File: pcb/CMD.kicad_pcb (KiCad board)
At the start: 2 copper layers, 37.6 x 53.4 mm, 87 parts, among them J1 Conn_01x06_Pin, J2 Conn_01x06_Socket

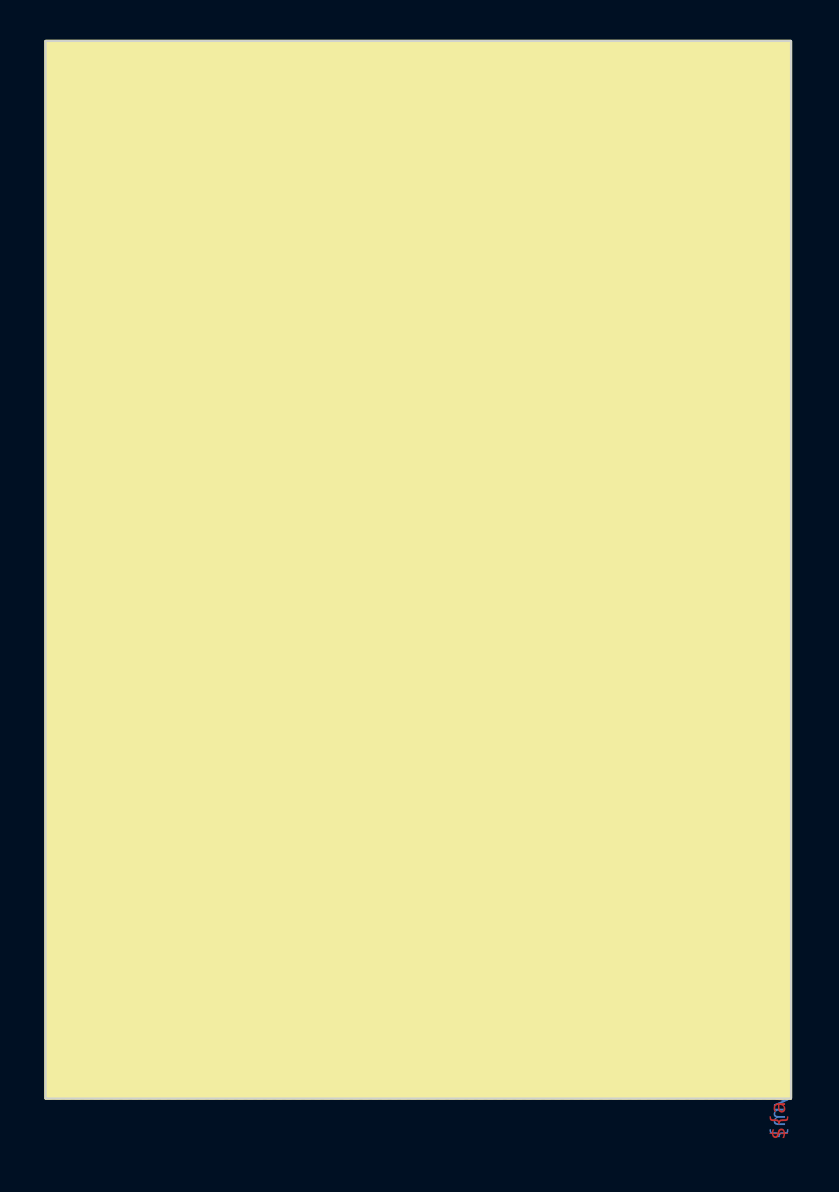
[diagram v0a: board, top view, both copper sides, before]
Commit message: Fix led position and add extended dimensioning
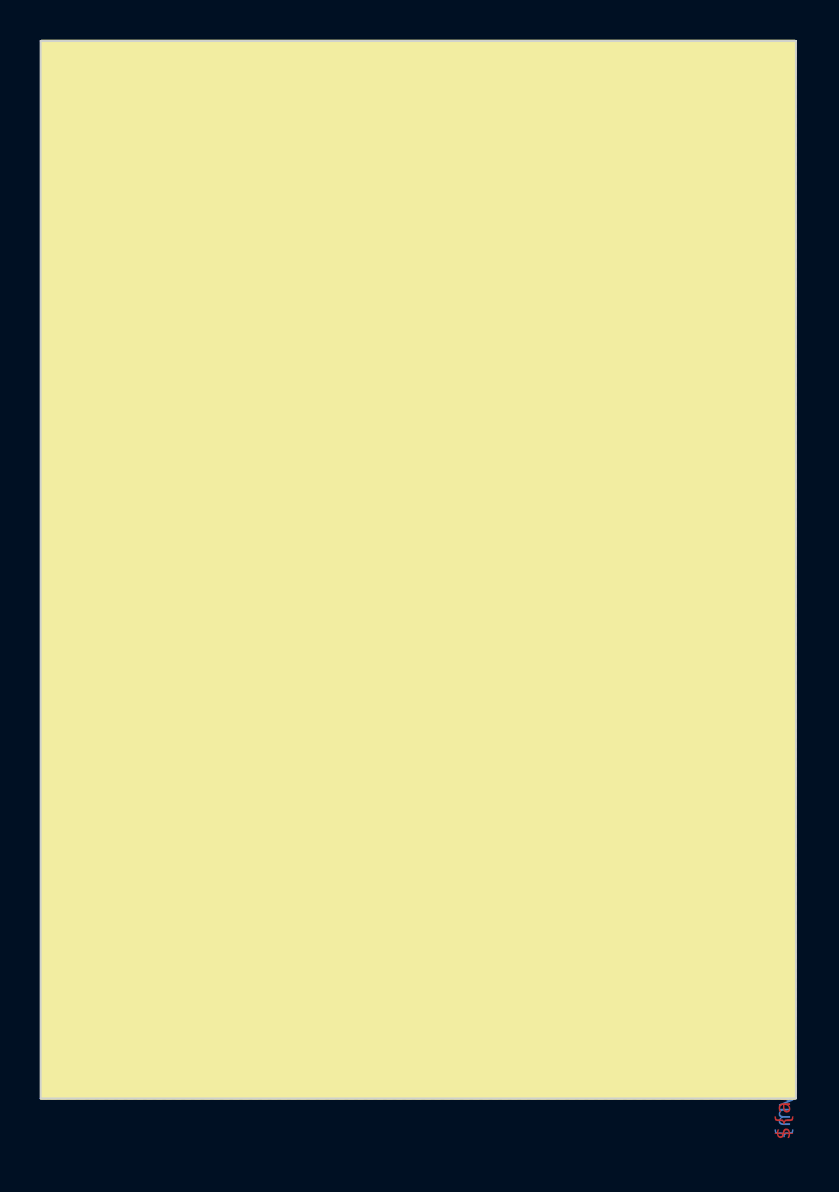
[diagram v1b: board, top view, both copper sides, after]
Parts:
- moved C29 0.25 mm to (159.6, 67.7)
- moved J2 0.25 mm to (160.8, 90.8)
- moved TP2 0.25 mm to (162.3, 113.0)
- moved C30 0.25 mm to (161.1, 77.5)
- moved C31 0.25 mm to (161.1, 80.6)
- moved C32 0.25 mm to (161.1, 100.3)
- moved C33 0.25 mm to (161.1, 102.9)
- moved C34 0.25 mm to (161.1, 107.4)
- moved D29 0.25 mm to (161.3, 67.3)
- moved D30 0.25 mm to (161.3, 74.9)
- moved D31 0.25 mm to (161.3, 82.5)
- moved D32 0.25 mm to (161.3, 90.2)
- moved D33 0.25 mm to (161.3, 97.8)
- moved D34 0.25 mm to (161.3, 105.4)
- moved D35 0.25 mm to (161.3, 113.0)
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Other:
- board size 37.6 x 53.4 mm -> 38.1 x 53.4 mm

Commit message: Lower pcb width
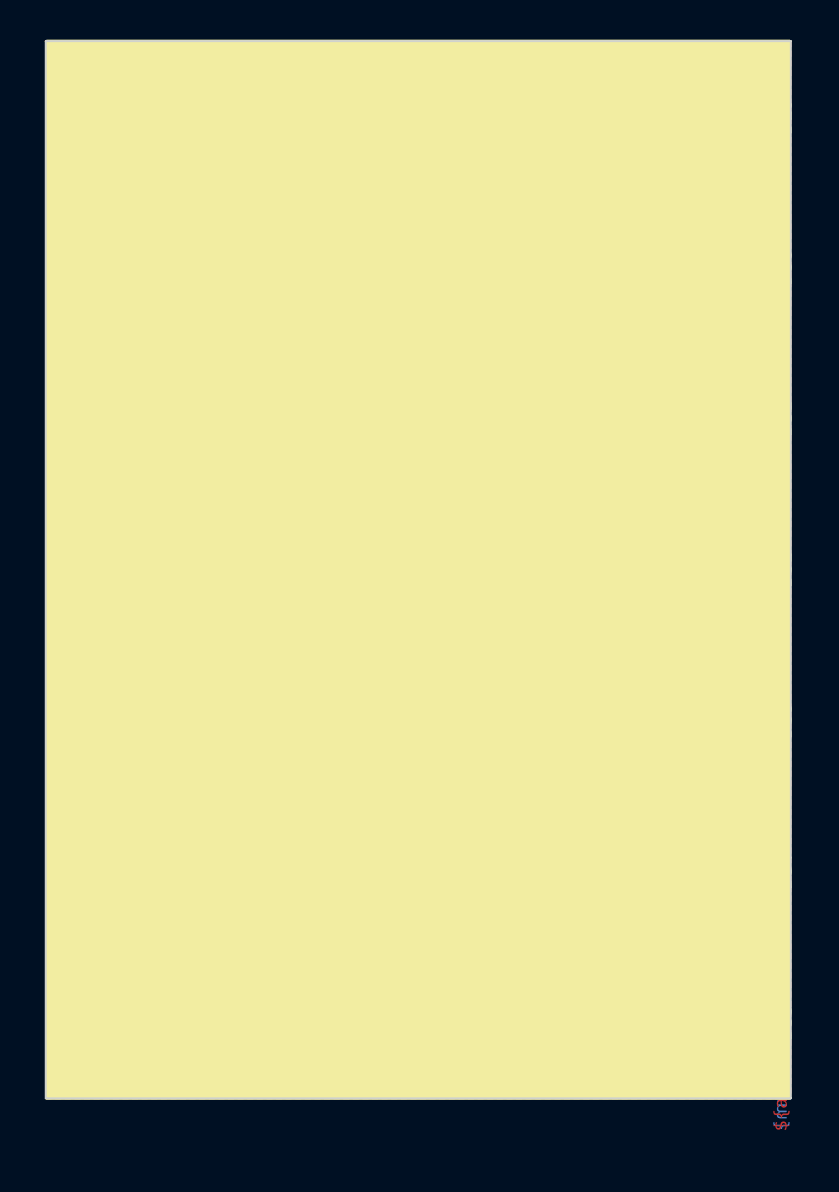
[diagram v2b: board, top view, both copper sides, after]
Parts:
- moved J1 0.26 mm to (128.3, 90.8)
- moved J2 0.25 mm to (160.5, 90.8)
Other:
- board size 38.1 x 53.4 mm -> 37.6 x 53.3 mm
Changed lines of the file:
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@@
     )
     (pad_to_mask_clearance 0)
-    (aux_axis_origin 127.004 63.495)
-    (grid_origin 127.004 63.495)
+    (aux_axis_origin 127.258 63.495)
+    (grid_origin 127.258 63.495)
     (pcbplotparams
       (layerselection 0x0010000_7ffffffe)
@@
   )
   (footprint "Connector_SMD:HARWIN_M20-8890645_Pin_Header" (layer "B.Cu")
-    (at 128.0415 90.796 90)
+    (at 128.2995 90.796 90)
     (property "Sheetfile" "CMD.kicad_sch")
     (property "Sheetname" "")
@@
   )
   (footprint "Connector_SMD:HARWIN_M20-7910642R_Pin_Socket" (layer "B.Cu")
-    (at 160.782 90.796 -90)
+    (at 160.532 90.796 -90)
     (property "Sheetfile" "CMD.kicad_sch")
     (property "Sheetname" "")
@@
   (gr_line (start 149.352 73.396) (end 145.542 73.396)
     (stroke (width 0.15) (type default)) (layer "B.SilkS"))
-  (gr_rect (start 127.054 63.495) (end 165.046 116.835)
+  (gr_rect (start 127.308 63.495) (end 164.792 116.835)
     (stroke (width 0.15) (type solid)) (fill solid) (layer "F.SilkS"))
-  (gr_rect (start 127 63.49) (end 165.1082 116.84)
+  (gr_rect (start 127.258 63.495) (end 164.85 116.835)
     (stroke (width 0.1) (type default)) (fill none) (layer "Edge.Cuts"))
   (gr_rect (start 120.904 83.053) (end 128.27 98.547)
     (stroke (width 0.15) (type default)) (fill none) (layer "User.1"))
-  (gr_text "${acronym}" (at 164.465 115.687 90) (layer "F.Cu")
-    (effects (font (size 0.75 0.75) (thickness 0.12)))
+  (gr_text "${acronym}" (at 164.342 115.687 90) (layer "F.Cu")
+    (effects (font (size 0.65 0.65) (thickness 0.12)))
   )
-  (gr_text "${acronym}" (at 164.465 115.687 90) (layer "B.Cu")
-    (effects (font (size 0.75 0.75) (thickness 0.12)) (justify mirror))
+  (gr_text "${acronym}" (at 164.342 115.687 90) (layer "B.Cu")
+    (effects (font (size 0.65 0.65) (thickness 0.12)) (justify mirror))
   )
   (gr_text "X" (at 141.478 87.112) (layer "B.SilkS")
@@
   )
   (dimension (type aligned) (layer "Dwgs.User")
-    (pts (xy 127.004 63.495) (xy 165.1042 63.495))
-    (height -3.81)
-    (gr_text "38.10" (at 146.0541 58.535) (layer "Dwgs.User")
+    (pts (xy 127.258 116.835) (xy 127.258 63.495))
+    (height -7.874)
+    (gr_text "53.34" (at 118.234 90.165 90) (layer "Dwgs.User")
       (effects (font (size 1 1) (thickness 0.15)))
     )
@@
   )
   (dimension (type aligned) (layer "Dwgs.User")
-    (pts (xy 127.254 63.495) (xy 127.254 116.84))
-    (height 11.43)
-    (gr_text "53.34" (at 114.674 90.1675 90) (layer "Dwgs.User")
-      (effects (font (size 1 1) (thickness 0.15)))
-    )
-    (format (prefix "") (suffix "") (units 3) (units_format 0) (precision 2))
-    (style (thickness 0.15) (arrow_length 1.27) (text_position_mode 0) (extension_height 0.58642) (extension_offset 0.5) keep_text_aligned)
-  )
-  (dimension (type aligned) (layer "User.1")
-    (pts (xy 130.81 113.025) (xy 127 113.025))
-    (height 50.8)
-    (gr_text "3.81" (at 128.905 61.075) (layer "User.1")
+    (pts (xy 127.258 63.495) (xy 164.8502 63.495))
+    (height -1.27)
+    (gr_text "37.59" (at 146.0541 61.075) (layer "Dwgs.User")
       (effects (font (size 1 1) (thickness 0.15)))
     )
@@
   )
   (dimension (type aligned) (layer "User.1")
-    (pts (xy 161.29 109.215) (xy 165.1 109.215))
-    (height -46.99)
-    (gr_text "3.81" (at 163.195 61.075) (layer "User.1")
+    (pts (xy 161.29 109.215) (xy 153.67 109.215))
+    (height 46.99)
+    (gr_text "7.62" (at 157.48 61.075) (layer "User.1")
       (effects (font (size 1 1) (thickness 0.15)))
     )
@@
   )
   (dimension (type aligned) (layer "User.1")
-    (pts (xy 161.29 109.215) (xy 153.67 109.215))
-    (height 46.99)
-    (gr_text "7.62" (at 157.48 61.075) (layer "User.1")
+    (pts (xy 161.29 113.025) (xy 164.85 113.025))
+    (height -50.8)
+    (gr_text "3.56" (at 163.07 61.075) (layer "User.1")
       (effects (font (size 1 1) (thickness 0.15)))
     )
@@
   )
   (dimension (type aligned) (layer "User.1")
+    (pts (xy 130.81 113.025) (xy 127.258 113.025))
+    (height 50.8)
+    (gr_text "3.56" (at 129.034 61.075) (layer "User.1")
+      (effects (font (size 1 1) (thickness 0.15)))
+    )
+    (format (prefix "") (suffix "") (units 3) (units_format 0) (precision 2) (override_value "3.56"))
+    (style (thickness 0.15) (arrow_length 1.27) (text_position_mode 0) (extension_height 0.58642) (extension_offset 0.5) keep_text_aligned)
+  )
+  (dimension (type aligned) (layer "User.1")
     (pts (xy 130.81 82.545) (xy 130.81 90.165))
     (height -37.084)
@@
   (segment (start 130.81 65.776) (end 130.81 64.905) (width 0.4) (layer "F.Cu") (net 5))
   (via (at 131.826 66.792) (size 0.4) (drill 0.3) (layers "F.Cu" "B.Cu") (net 5))
+  (segment (start 133.984 92.066) (end 131.9145 92.066) (width 0.4) (layer "B.Cu") (net 5))
   (segment (start 131.826 66.792) (end 133.35 66.792) (width 0.4) (layer "B.Cu") (net 5))
   (segment (start 135.128 68.57) (end 135.128 90.922) (width 0.4) (layer "B.Cu") (net 5))
-  (segment (start 135.128 90.922) (end 133.984 92.066) (width 0.4) (layer "B.Cu") (net 5))
-  (segment (start 133.984 92.066) (end 131.826 92.066) (width 0.4) (layer "B.Cu") (net 5))
   (segment (start 133.35 66.792) (end 135.128 68.57) (width 0.4) (layer "B.Cu") (net 5))
-  (segment (start 131.826 94.606) (end 153.303 94.606) (width 0.4) (layer "B.Cu") (net 6))
+  (segment (start 135.128 90.922) (end 133.984 92.066) (width 0.4) (layer "B.Cu") (net 5))
+  (segment (start 131.9145 94.606) (end 153.307 94.606) (width 0.4) (layer "B.Cu") (net 6))
   (segment (start 130.81 77.325) (end 130.81 80.145) (width 0.8) (layer "F.Cu") (net 7))
   (segment (start 132.51 77.325) (end 132.51 80.145) (width 0.8) (layer "F.Cu") (net 8))
@@
   (via (at 161.163 113.782) (size 0.4) (drill 0.3) (layers "F.Cu" "B.Cu") (net 36))
   (segment (start 156.972 109.591) (end 156.972 93.462) (width 0.4) (layer "B.Cu") (net 36))
+  (segment (start 161.163 113.782) (end 156.972 109.591) (width 0.4) (layer "B.Cu") (net 36))
   (segment (start 156.972 93.462) (end 155.576 92.066) (width 0.4) (layer "B.Cu") (net 36))
-  (segment (start 157.226 109.845) (end 156.972 109.591) (width 0.4) (layer "B.Cu") (net 36))
-  (segment (start 161.163 113.782) (end 157.226 109.845) (width 0.4) (layer "B.Cu") (net 36))
-  (segment (start 155.576 92.066) (end 153.303 92.066) (width 0.4) (layer "B.Cu") (net 36))
+  (segment (start 155.576 92.066) (end 153.307 92.066) (width 0.4) (layer "B.Cu") (net 36))
   (segment (start 146.05 80.145) (end 146.05 77.325) (width 0.8) (layer "F.Cu") (net 37))
   (segment (start 147.75 80.145) (end 147.75 77.325) (width 0.8) (layer "F.Cu") (net 38))
   (segment (start 146.05 87.765) (end 146.05 84.945) (width 0.8) (layer "F.Cu") (net 39))
-  (segment (start 131.91 84.362) (end 131.826 84.446) (width 1) (layer "B.Cu") (net 40))
   (segment (start 131.91 81.651) (end 131.91 84.362) (width 1) (layer "B.Cu") (net 40))
   (segment (start 147.75 87.765) (end 147.75 84.945) (width 0.8) (layer "F.Cu") (net 41))
@@
   (via (at 163.068 113.782) (size 0.4) (drill 0.3) (layers "F.Cu" "B.Cu") (net 78))
   (segment (start 157.988 108.702) (end 157.988 91.43) (width 0.4) (layer "B.Cu") (net 78))
-  (segment (start 157.988 91.43) (end 156.084 89.526) (width 0.4) (layer "B.Cu") (net 78))
-  (segment (start 156.084 89.526) (end 153.303 89.526) (width 0.4) (layer "B.Cu") (net 78))
   (segment (start 163.068 113.782) (end 157.988 108.702) (width 0.4) (layer "B.Cu") (net 78))
+  (segment (start 157.988 91.43) (end 156.084 89.526) (width 0.4) (layer "B.Cu") (net 78))
+  (segment (start 156.084 89.526) (end 153.307 89.526) (width 0.4) (layer "B.Cu") (net 78))
   (zone (net 2) (net_name "GND") (layers "F&B.Cu") (hatch edge 0.5)
     (connect_pads yes (clearance 0.25))
@@
     (polygon
       (pts
-        (xy 127.004 63.495)
-        (xy 165.1042 63.495)
-        (xy 165.1042 116.845)
-        (xy 127.004 116.845)
+        (xy 127.258 63.495)
+        (xy 164.8502 63.495)
+        (xy 164.8502 116.845)
+        (xy 127.258 116.845)
       )
     )
